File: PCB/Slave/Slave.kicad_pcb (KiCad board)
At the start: 2 copper layers, 54.2 x 45.3 mm, 55 parts, among them J1 USB_C_Receptacle_USB2.0_16P, J2 Conn_01x05_Pin, J3 Conn_01x07_Socket, J4 Conn_01x04_Socket, J5 Conn_01x07_Socket, Q2 PNP, SW1 PTS810_SJM_250_SMTR_LFS, SW2 PTS810_SJM_250_SMTR_LFS, U1 ESP32-S3-MINI-1, U2 TCA9406DC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

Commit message: PCB-Update
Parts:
- added ?: , , F.Cu at (32.3, 58.4)
- added ?: , , F.Cu at (32.2, 56.9)
- added ?: , , F.Cu at (32.2, 56.1)
- added ?: , , F.Cu at (30.7, 56.9)
- added ?: , , F.Cu at (30.7, 58.4)
- added ?: , , F.Cu at (32.2, 57.6)
- added ?: , , F.Cu at (30.7, 56.1)
- added ?: , , F.Cu at (30.7, 57.6)
- moved R17 0.28 mm to (56.9, 79.8)
- moved R16 0.27 mm to (58.4, 78.2)
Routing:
- net VCC_5V: track 126.7 -> 127.6 mm, vias 6 -> 5
- net CAN+: track 28.0 -> 27.2 mm

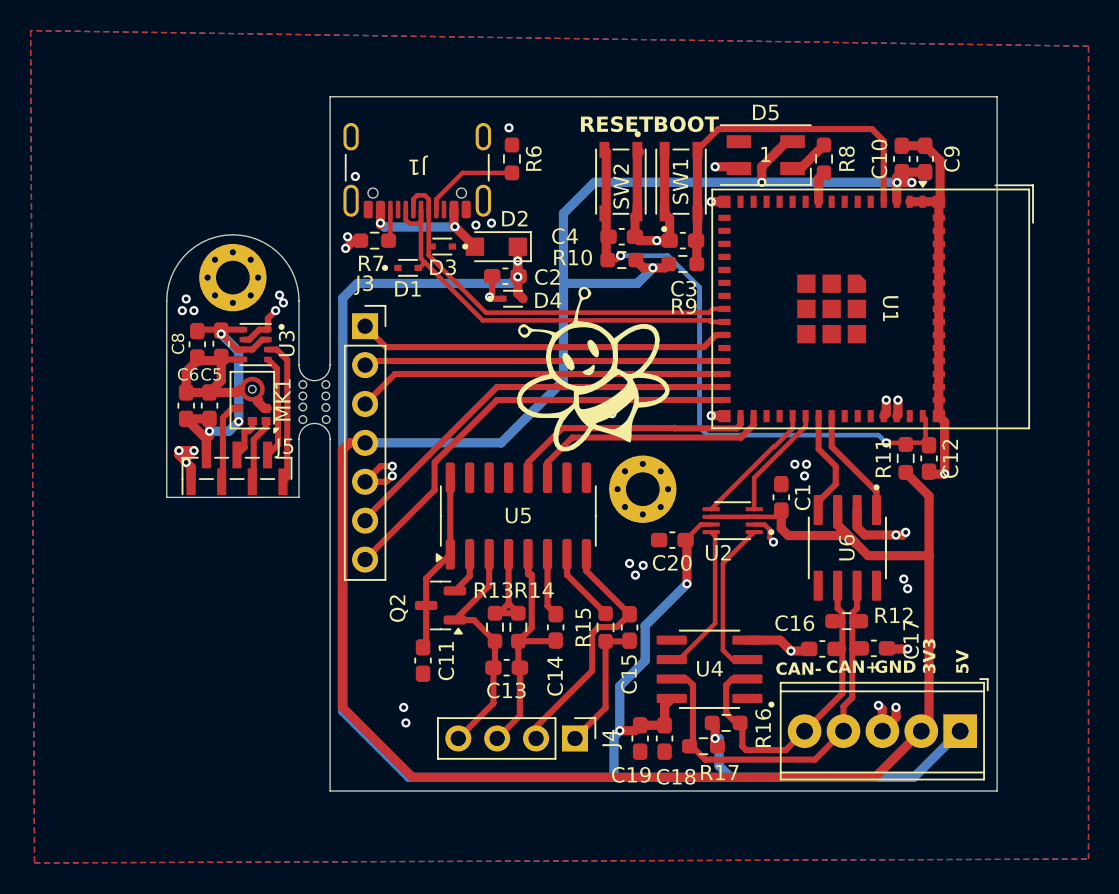
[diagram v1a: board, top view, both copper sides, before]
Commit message: Small changes to the pcb(Master and Slave))
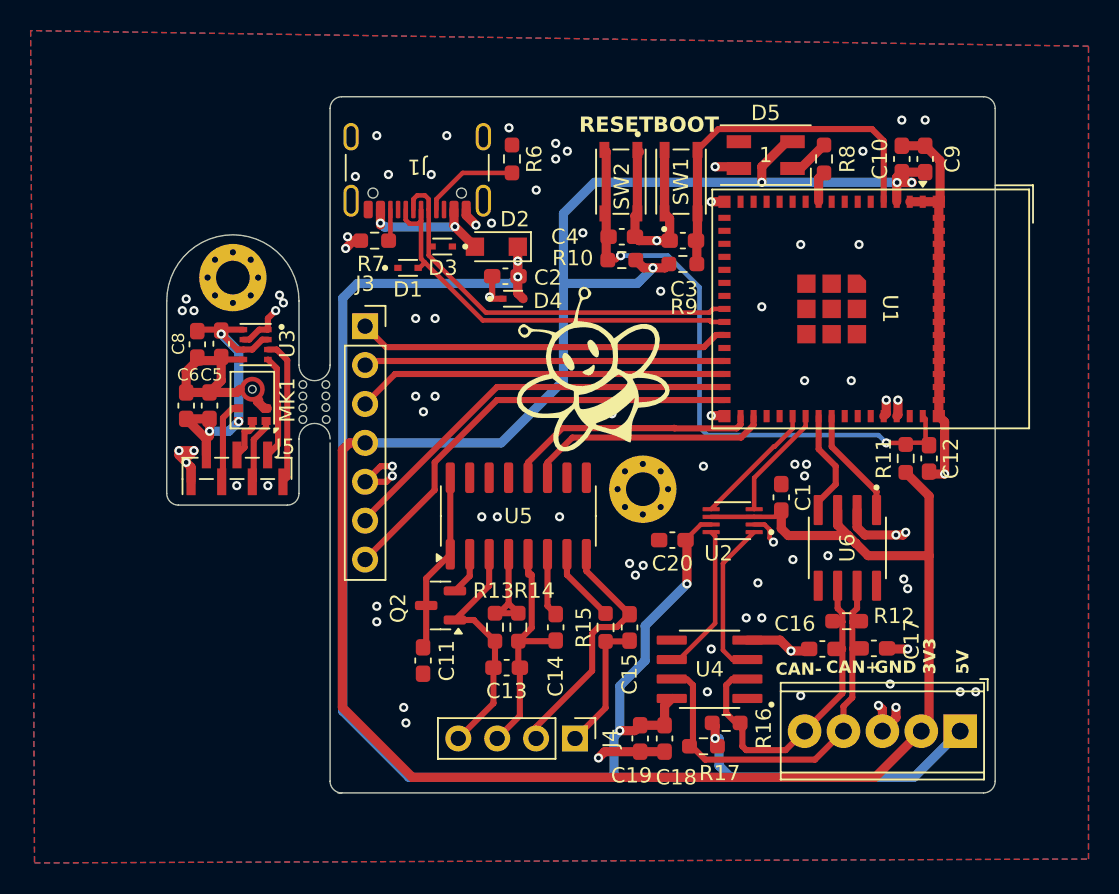
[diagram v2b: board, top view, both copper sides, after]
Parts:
- C1: value u1F -> 100nF
- C19, C3, C4, C5, C7, C9: value 0u1F -> 100nF
- moved ? 0.06 mm to (30.7, 57.7)
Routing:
- net GND_OUT: track 90.2 -> 95.9 mm, vias 43 -> 86
- net ESP_3V3: track 184.3 -> 182.9 mm
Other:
- board size 54.2 x 45.3 mm -> 54.1 x 45.5 mm

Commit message: Added CAP
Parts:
- added C21: 100nF, Capacitor_SMD:C_0603_1608Metric_Pad1.08x0.95mm_HandSolder, F.Cu at (71.4, 68.6)
- added C22: 1uF, Capacitor_SMD:C_0603_1608Metric_Pad1.08x0.95mm_HandSolder, F.Cu at (69.8, 68.6)
- added C23: 100nF, Capacitor_SMD:C_0603_1608Metric_Pad1.08x0.95mm_HandSolder, F.Cu at (54.9, 67.8)
- added C24: u1F, Capacitor_SMD:C_0603_1608Metric_Pad1.08x0.95mm_HandSolder, F.Cu at (62.2, 66.8)
- moved C2 0.59 mm to (44.6, 49.1)
- moved D4 0.59 mm to (45.0, 50.5)
- moved D2 0.57 mm to (43.9, 47.1)
- moved C1 0.25 mm to (62.2, 63.5)
- moved D3 0.08 mm to (39.8, 47.1)
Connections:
- C11 pad 1: Net-(Q2-E) -> ESP_3V3
- Q2 pad 3: Net-(Q2-E) -> ESP_3V3
- U5 pad 1: Net-(Q2-E) -> ESP_3V3
- U5 pad 16: Net-(Q2-E) -> ESP_3V3
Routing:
- net ESP_3V3: track 182.9 -> 200.0 mm, vias 7 -> 9
- net GND_OUT: track 95.9 -> 108.8 mm, vias 86 -> 95
- net Net-(Q2-E): track 11.8 -> 0.00 mm
- net VCC_5V: track 127.6 -> 128.6 mm
- net CAN+: track 27.2 -> 26.4 mm
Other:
- outline, holes or cut-outs redrawn

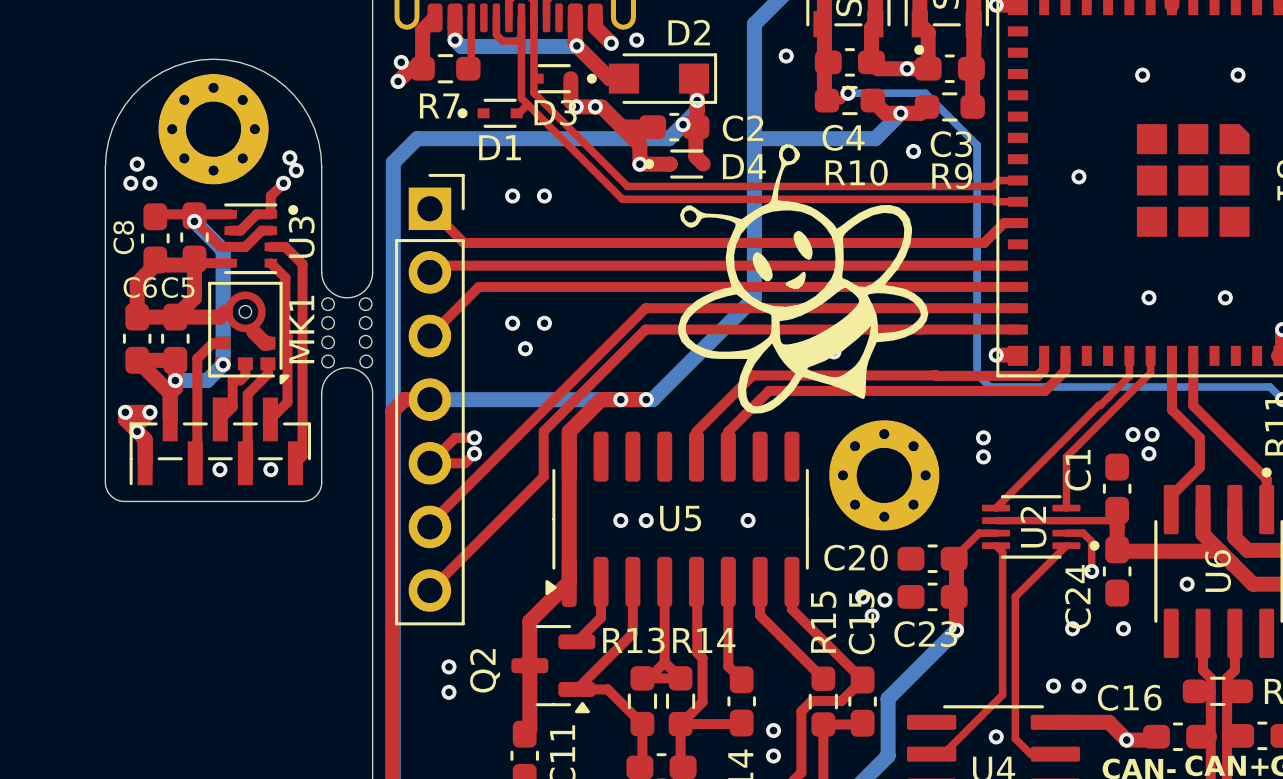
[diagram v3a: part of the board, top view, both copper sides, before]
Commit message: Changed bmp for bme
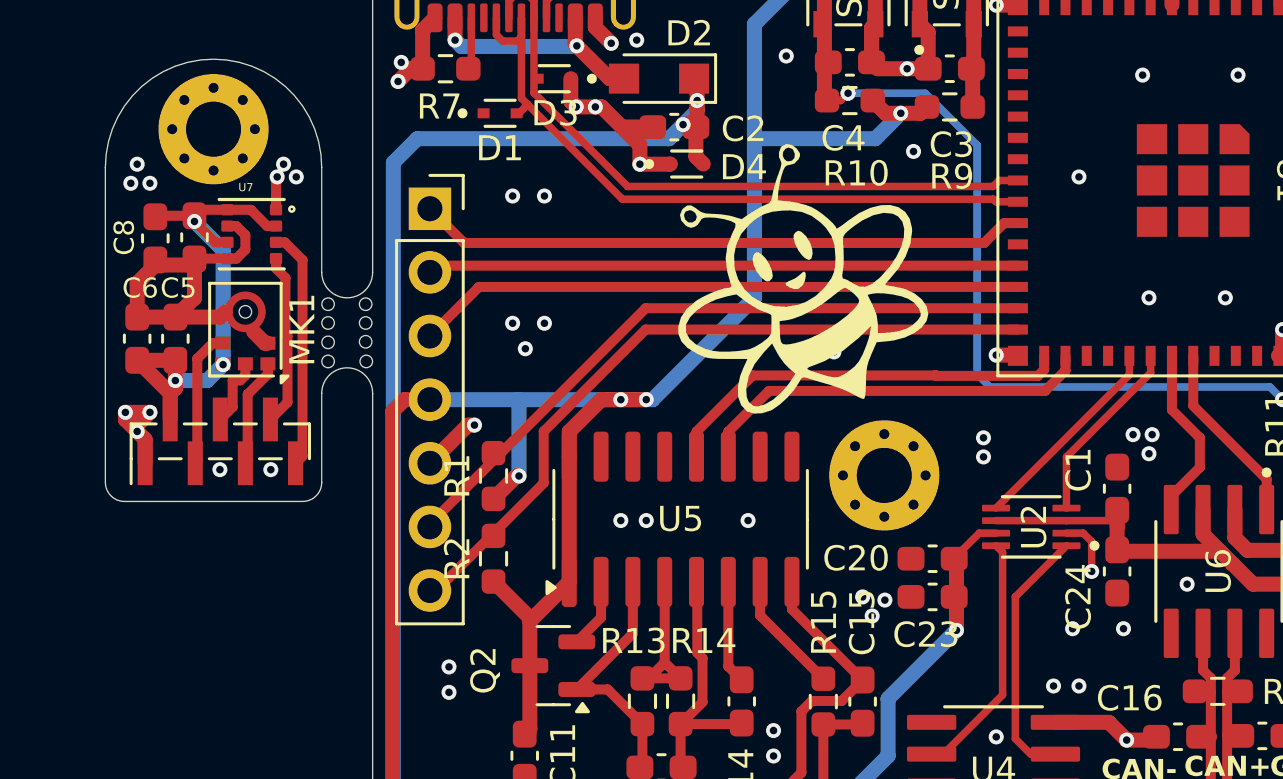
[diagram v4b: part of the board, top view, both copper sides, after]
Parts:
- removed U3: BMP280, BMP280:XDCR_BMP280
- added R1: 4k7, Resistor_SMD:R_0603_1608Metric_Pad0.98x0.95mm_HandSolder, F.Cu at (37.3, 63.0)
- added R2: 4k7, Resistor_SMD:R_0603_1608Metric_Pad0.98x0.95mm_HandSolder, F.Cu at (37.3, 66.3)
- added U7: BME280, BME280:PSON65P250X250X100-8N, F.Cu at (27.7, 53.3)
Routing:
- net ESP_3V3: track 200.0 -> 206.9 mm, vias 9 -> 10
- net GND_OUT: track 108.8 -> 107.3 mm, vias 95 -> 94

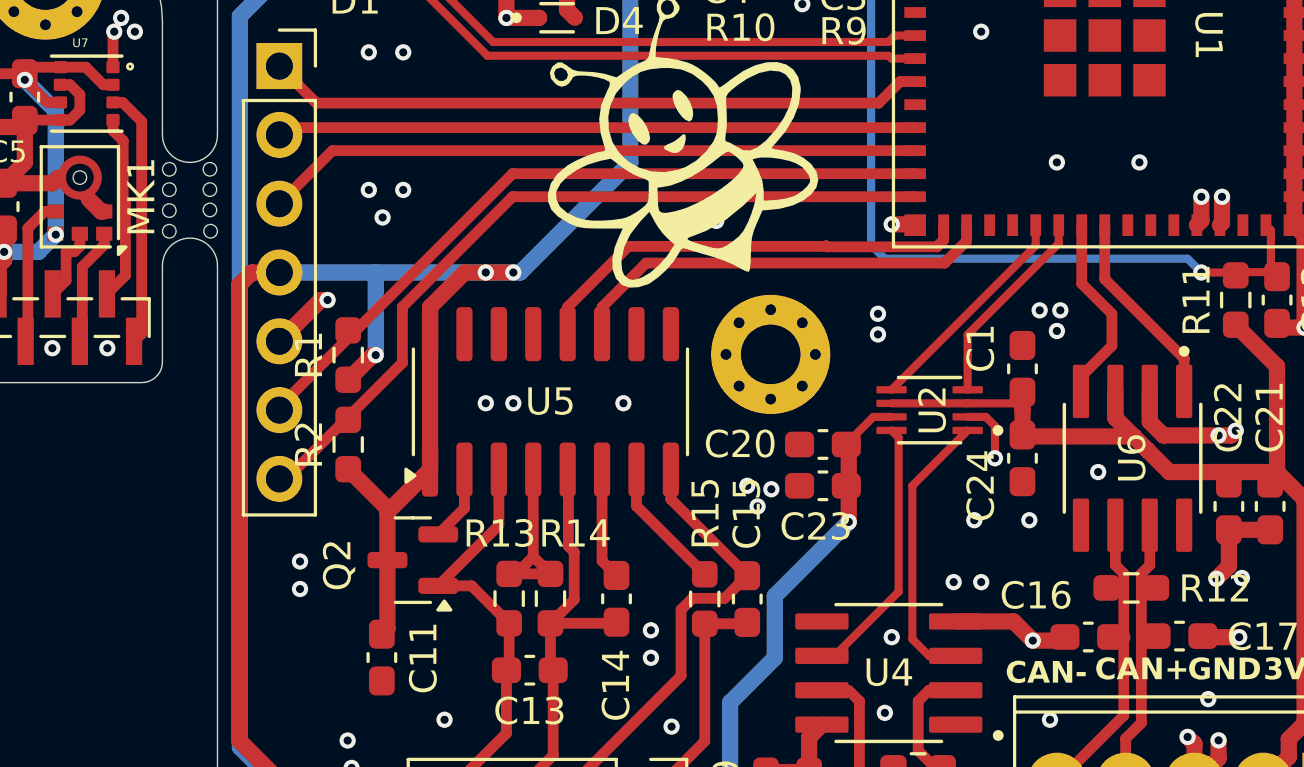
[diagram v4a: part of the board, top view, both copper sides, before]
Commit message: Added I2C PullUp Resistors
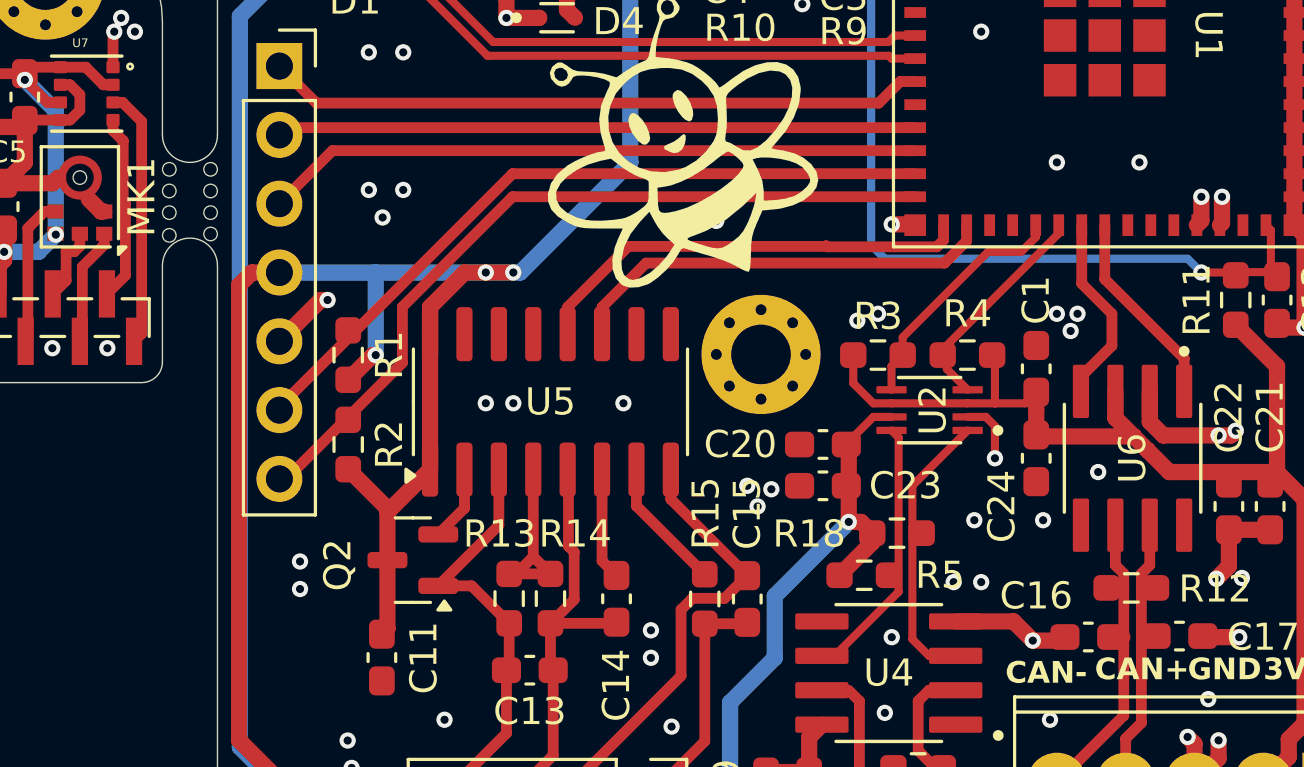
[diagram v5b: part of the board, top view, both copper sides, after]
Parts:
- removed the ? at (32.3, 58.4)
- removed the ? at (30.7, 56.9)
- removed the ? at (30.7, 58.4)
- removed the ? at (30.7, 57.7)
- removed the ? at (32.2, 56.1)
- removed the ? at (32.2, 57.6)
- removed the ? at (32.2, 56.9)
- added ?: , , F.Cu at (30.7, 57.7)
- added ?: , , F.Cu at (32.3, 56.1)
- added ?: , , F.Cu at (30.7, 58.6)
- added ?: , , F.Cu at (32.3, 58.5)
- added ?: , , F.Cu at (32.3, 56.9)
- added ?: , , F.Cu at (32.3, 57.7)
- added ?: , , F.Cu at (30.7, 56.9)
- added R18: 4k7, Resistor_SMD:R_0603_1608Metric_Pad0.98x0.95mm_HandSolder, F.Cu at (57.6, 69.6)
- added R3: 4k7, Resistor_SMD:R_0603_1608Metric_Pad0.98x0.95mm_HandSolder, F.Cu at (56.9, 63.0)
- added R4: 4k7, Resistor_SMD:R_0603_1608Metric_Pad0.98x0.95mm_HandSolder, F.Cu at (60.2, 63.0)
- added R5: 4k7, Resistor_SMD:R_0603_1608Metric_Pad0.98x0.95mm_HandSolder, F.Cu at (56.4, 71.1)
- moved C1 0.51 mm to (62.7, 63.5)
- moved C24 0.51 mm to (62.7, 66.8)
- moved H1 0.36 mm to (52.6, 63.0)
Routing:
- net ESP_3V3: track 206.9 -> 211.9 mm
- net VCC_5V: track 128.6 -> 131.7 mm
- net SDA_ESP: track 7.47 -> 8.23 mm
- net SCL_ESP: track 8.28 -> 9.00 mm

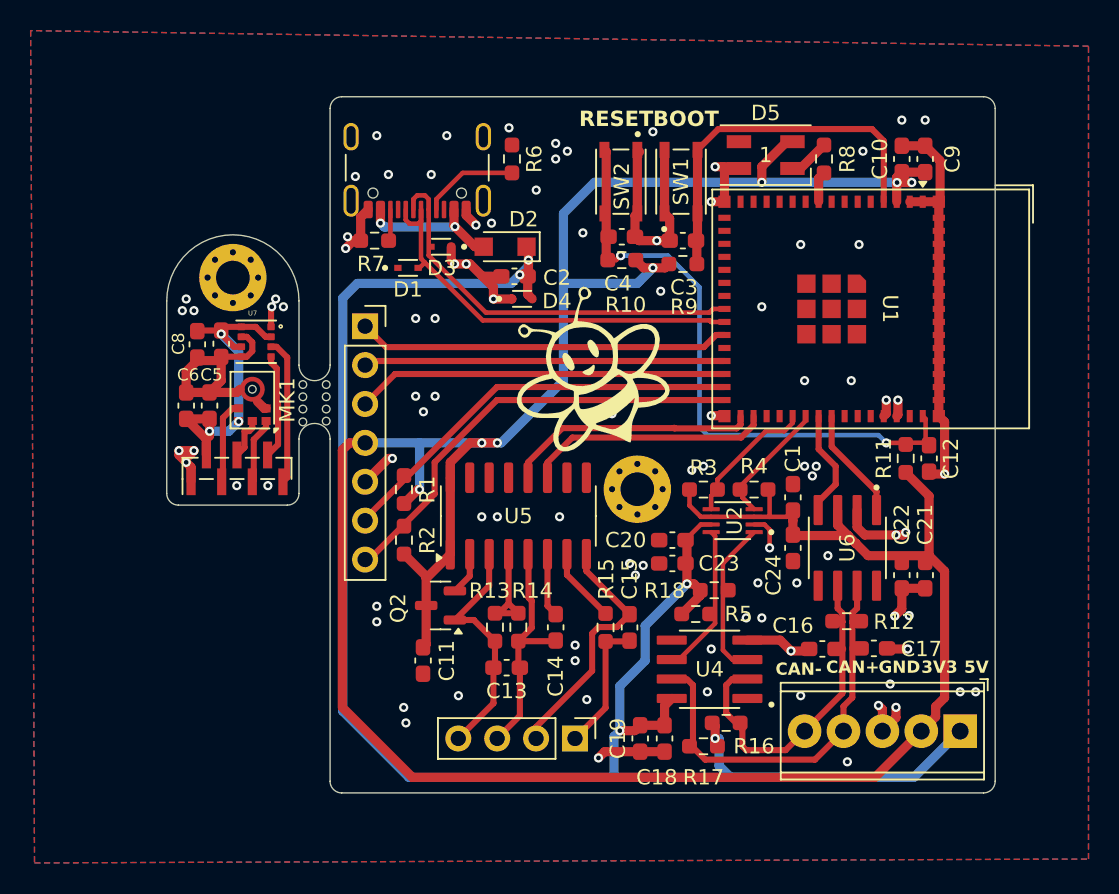
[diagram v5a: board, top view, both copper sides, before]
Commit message: repaired HX711
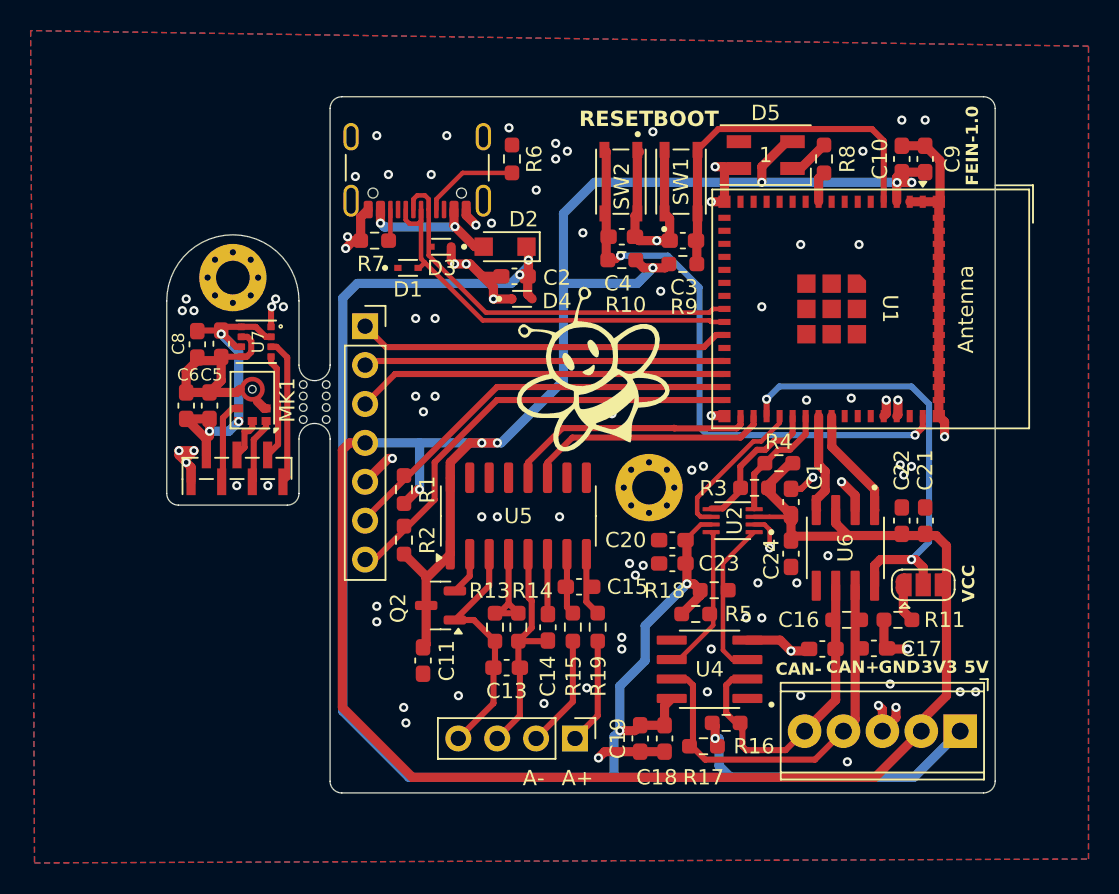
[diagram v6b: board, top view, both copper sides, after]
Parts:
- removed the ? at (30.7, 57.7)
- removed the ? at (30.7, 58.6)
- removed the ? at (32.3, 58.5)
- removed the ? at (32.3, 56.9)
- removed the ? at (32.3, 57.7)
- removed the ? at (30.7, 56.1)
- removed the ? at (30.7, 56.9)
- removed C12: 1uf, Capacitor_SMD:C_0603_1608Metric_Pad1.08x0.95mm_HandSolder
- added ?: , , F.Cu at (30.8, 58.4)
- added ?: , , F.Cu at (30.8, 56.1)
- added ?: , , F.Cu at (30.8, 56.9)
- added ?: , , F.Cu at (30.8, 57.6)
- added ?: , , F.Cu at (32.3, 57.6)
- added ?: , , F.Cu at (32.3, 56.9)
- added ?: , , F.Cu at (32.3, 58.4)
- added JP1: SolderJumper_3_Open, Jumper:SolderJumper-3_P1.3mm_Open_RoundedPad1.0x1.5mm, F.Cu at (71.2, 69.2)
- added R19: 100, Resistor_SMD:R_0603_1608Metric_Pad0.98x0.95mm_HandSolder, F.Cu at (50.0, 72.0)
- C11, C13: value 1uF -> 10uF
- C14: value 1uF -> 100nF
- C4: value 100nF -> 1uF
- R11: value 10k -> R
- R15: value 1k -> 100
- moved R11 10.6 mm to (69.6, 71.5), turned to 0 degrees
- moved C15 4.24 mm to (48.8, 69.3), turned to 180 degrees
- moved C21 3.56 mm to (71.4, 65.0), turned to 90 degrees
- moved C22 3.56 mm to (69.8, 65.0), turned to 90 degrees
- moved R3 3.34 mm to (60.2, 62.9), turned to 180 degrees
- moved R4 2.37 mm to (61.8, 61.3)
- moved R15 2.14 mm to (48.4, 72.0)
- moved H1 0.77 mm to (53.3, 62.9)
- moved C14 0.51 mm to (46.7, 72.0)
- moved C24 0.40 mm to (62.6, 67.2)
- moved C1 0.33 mm to (62.6, 63.8)
- moved U6 0.13 mm to (66.2, 66.8)
- moved R12 0.09 mm to (66.2, 71.5)
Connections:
- C13 pad 2: Net-(J4-Pin_3) -> GND_OUT
- C14 pad 2: Net-(J4-Pin_3) -> GND_OUT
- C15 pad 1: Net-(J4-Pin_2) -> Net-(U5-INA+)
- C15 pad 2: Net-(J4-Pin_1) -> Net-(U5-INA-)
- J4 pad 3: Net-(J4-Pin_3) -> GND_OUT
- R11 pad 1: ESP_3V3 -> GND_OUT
- R11 pad 2: CHIP_PU -> Net-(JP1-A)
- R14 pad 1: Net-(J4-Pin_3) -> GND_OUT
- R15 pad 1: Net-(J4-Pin_1) -> Net-(J4-Pin_2)
- U1 pad 33: unconnected-(U1-IO37-Pad33) -> CAN_RS
- U1 pad 34: unconnected-(U1-IO38-Pad34) -> I2C_OE
- U2 pad 6: ESP_3V3 -> I2C_OE
- U5 pad 10: unconnected-(U5-INB+-Pad10) -> GND_OUT
- U5 pad 5: Net-(J4-Pin_3) -> GND_OUT
- U5 pad 8: Net-(J4-Pin_2) -> Net-(U5-INA+)
- U5 pad 9: unconnected-(U5-INB--Pad9) -> GND_OUT
- U6 pad 8: unconnected-(U6-RS-Pad8) -> CAN_RS
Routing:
- net CAN_RS: track 0.00 -> 29.2 mm, vias 0 -> 2
- net Net-(J4-Pin_3): track 15.6 -> 0.00 mm
- net I2C_OE: track 0.00 -> 9.88 mm
- net GND_OUT: track 107.3 -> 116.4 mm, vias 94 -> 93
- net Net-(J4-Pin_2): track 16.4 -> 7.36 mm
- net ESP_3V3: track 211.9 -> 204.6 mm
- net Net-(U5-INA+): track 0.00 -> 4.15 mm
- net Net-(JP1-A): track 0.00 -> 2.52 mm
- net CAN-: track 23.0 -> 21.0 mm
- net CHIP_PU: track 41.2 -> 39.3 mm
- net Net-(J4-Pin_1): track 8.75 -> 6.97 mm
- net CAN+: track 26.4 -> 25.4 mm
- net Net-(U5-INA-): track 4.91 -> 4.00 mm
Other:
- board text added: "A+"
- board text added: "A-"
- board text added: "FEIN-1.0"
- board text added: "VCC"
